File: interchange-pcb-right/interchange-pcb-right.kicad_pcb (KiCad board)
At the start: 2 copper layers, 175.6 x 104 mm, 156 parts, among them J1 Conn_01x04, J2 Conn_01x04, J3 TRRS_L, J4 TRRS_R, J5 SSD1306, SW1 RotaryEncoder, U1 Seeeduino Xiao rp2040, U2 PCA9555PW, U3 PCA9555PW, U4 ADS1110, U6 TCA4307DGKR

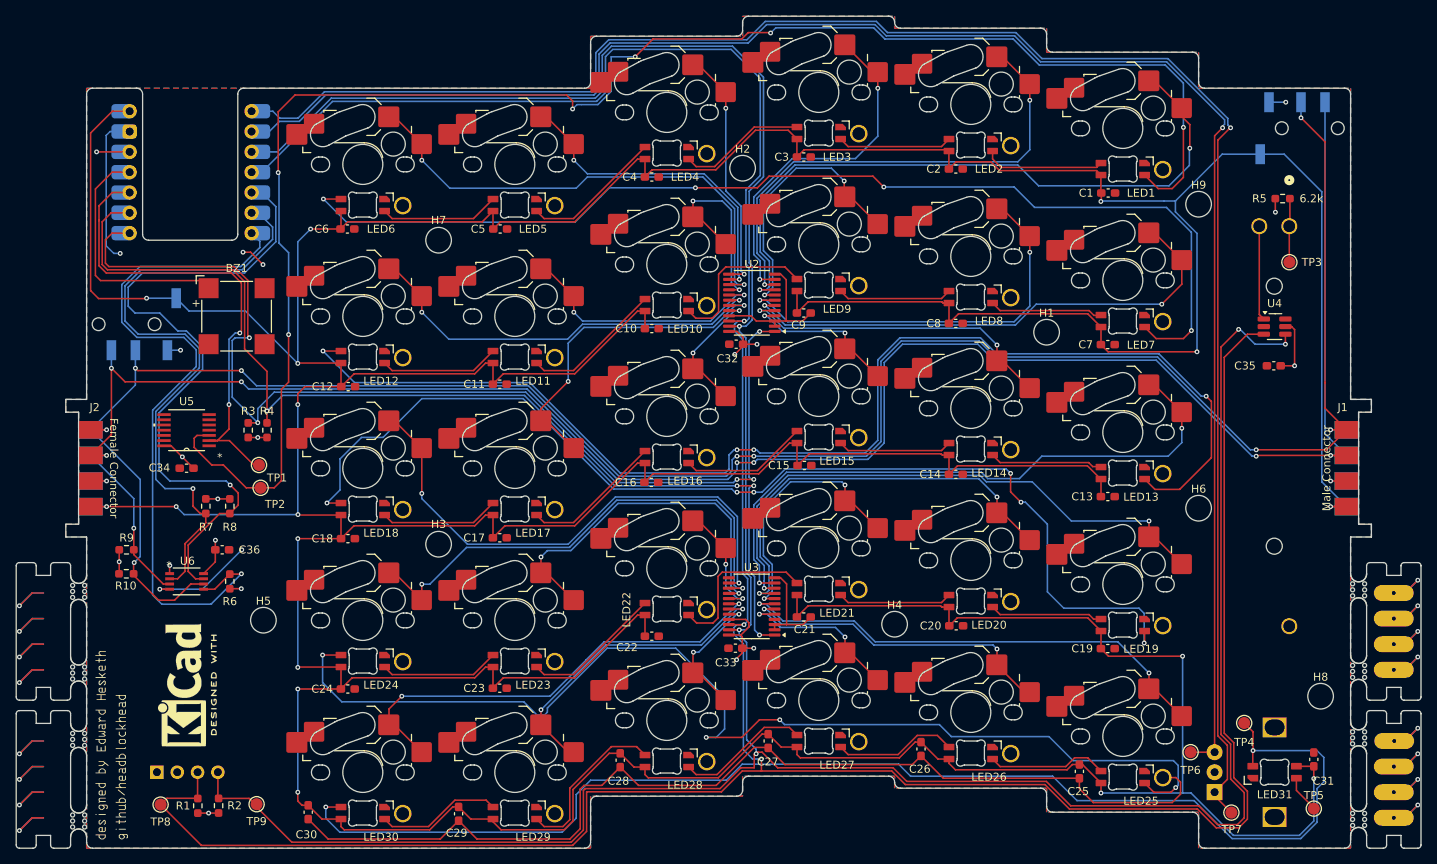
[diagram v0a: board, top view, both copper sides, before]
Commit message: feat: round connector pads, add resistor values + silkscreen gfx
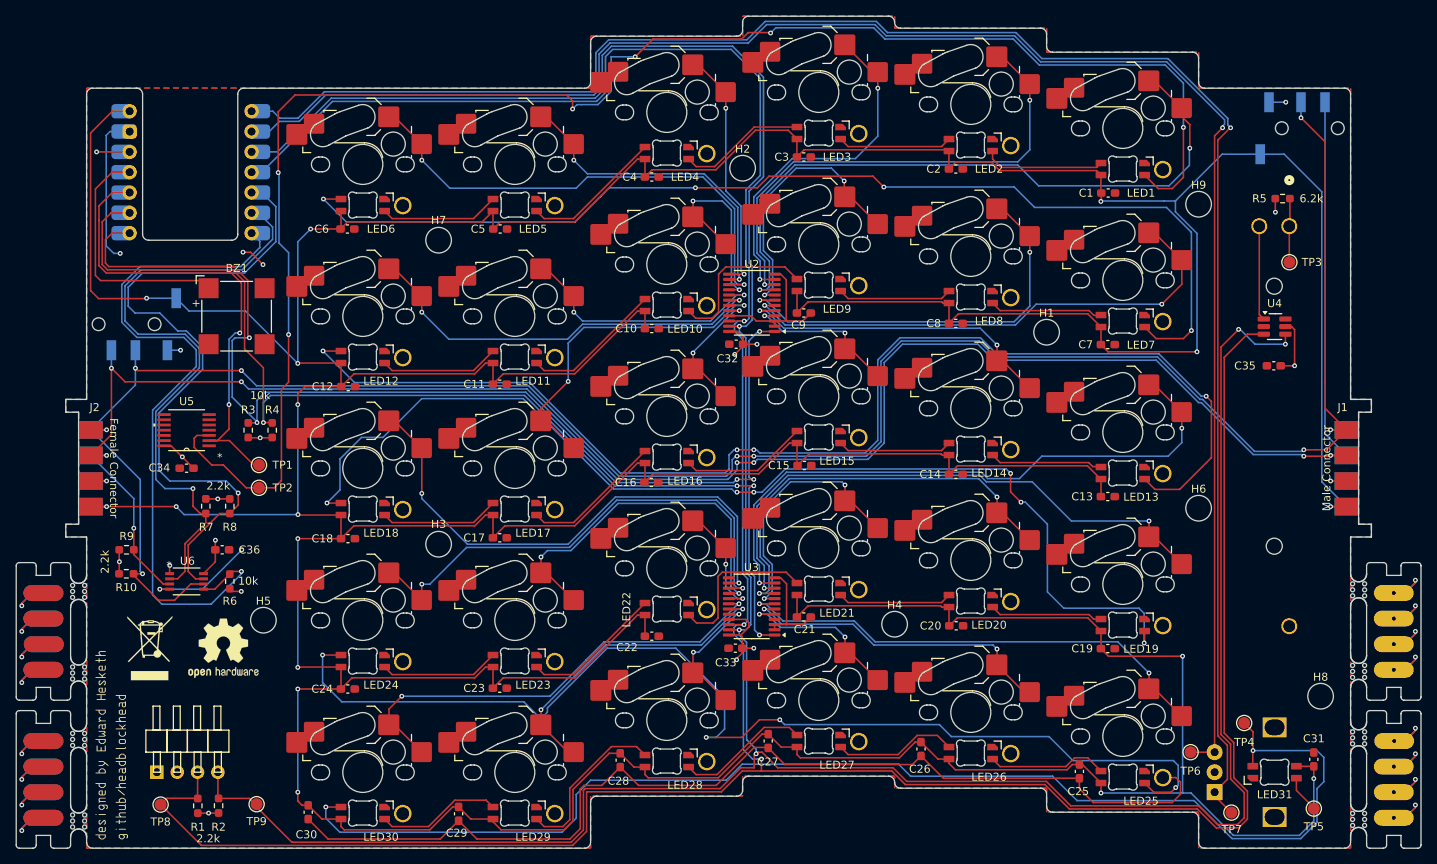
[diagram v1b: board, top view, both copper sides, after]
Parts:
- removed the REF** at (81.9, 129.6)
- added REF**: WEEE-Logo_5.6x8mm_SilkScreen, Symbol:WEEE-Logo_5.6x8mm_SilkScreen, F.Cu at (77.9, 125.0)
- added REF**: Pogo_Pad, CustomFootprints:Pogo_Pad, F.Cu at (64.6, 121.3)
- added REF**: Pogo_Pad, CustomFootprints:Pogo_Pad, F.Cu at (64.6, 143.0)
- added REF**: Pogo_Pad, CustomFootprints:Pogo_Pad, F.Cu at (64.6, 127.7)
- added REF**: Pogo_Pad, CustomFootprints:Pogo_Pad, F.Cu at (64.7, 124.5)
- added REF**: OSHW-Logo2_9.8x8mm_SilkScreen, Symbol:OSHW-Logo2_9.8x8mm_SilkScreen, F.Cu at (87.1, 125.0)
- added REF**: Pogo_Pad, CustomFootprints:Pogo_Pad, F.Cu at (64.6, 139.8)
- added REF**: Pogo_Pad, CustomFootprints:Pogo_Pad, F.Cu at (64.6, 118.1)
- added REF**: Pogo_Pad, CustomFootprints:Pogo_Pad, F.Cu at (64.6, 146.2)
- added REF**: Pogo_Pad, CustomFootprints:Pogo_Pad, F.Cu at (64.6, 136.6)
- U5: value (none) -> SN74AHCT125PWR
- moved R4 0.65 mm to (93.2, 97.8)
- moved TP2 0.20 mm to (91.5, 105.0)
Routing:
- net (no net): track 117.2 -> 113.2 mm
- net /EXPANDER2_INT: track 134.6 -> 138.0 mm
- net /I2C_BUS_SDA: track 272.9 -> 273.9 mm
- net +3V3: track 57.1 -> 57.9 mm
- net /EXPANDER1_INT: track 138.3 -> 138.8 mm
